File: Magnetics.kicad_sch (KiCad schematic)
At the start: 1 part, among them U1 AS5600

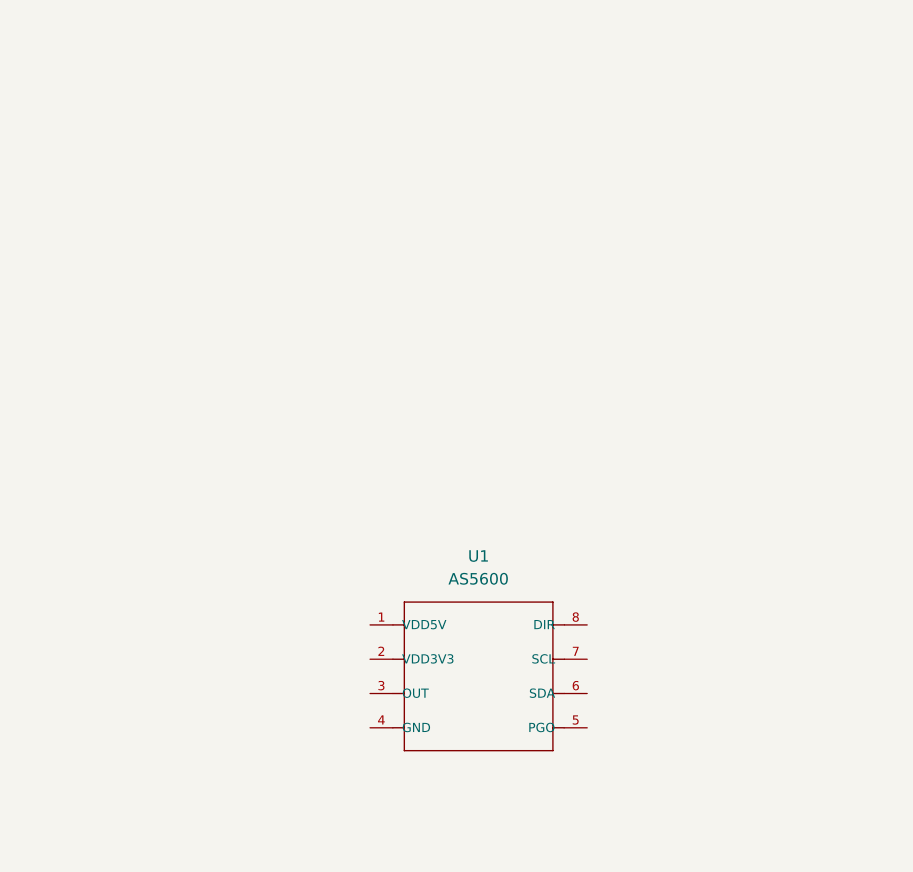
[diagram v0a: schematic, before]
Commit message: Schematic done
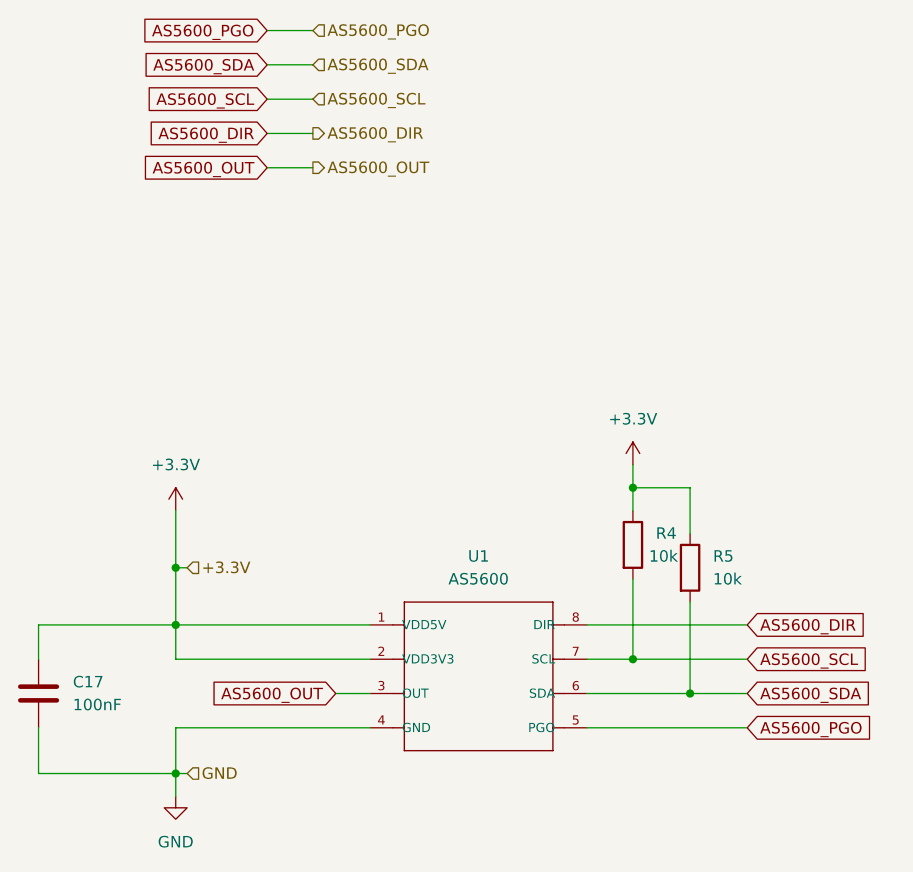
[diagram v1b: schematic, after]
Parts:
- added C17: 100nF, Capacitor_SMD:C_0603_1608Metric_Pad1.08x0.95mm_HandSolder, symbol Device:C
- added R4, R5: 10k, Resistor_SMD:R_0603_1608Metric_Pad0.98x0.95mm_HandSolder, symbol Device:R
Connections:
- net +3.3V: now reaches U1.1 (VDD5V)
- net +3.3V: now also U1.2 (VDD3V3), C17.1, R4.1, R5.1
- net AS5600_OUT: now reaches U1.3 (OUT)
- net GND: now reaches U1.4 (GND)
- net GND: now also C17.2
- net AS5600_PGO: now reaches U1.5 (PGO)
- net AS5600_SDA: now reaches U1.6 (SDA)
- net AS5600_SDA: now also R5.2
- net AS5600_SCL: now reaches U1.7 (SCL)
- net AS5600_SCL: now also R4.2
- net AS5600_DIR: now reaches U1.8 (DIR)
